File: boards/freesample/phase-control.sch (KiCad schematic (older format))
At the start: 45 parts, among them U16 HMC856, U17 NB6L295

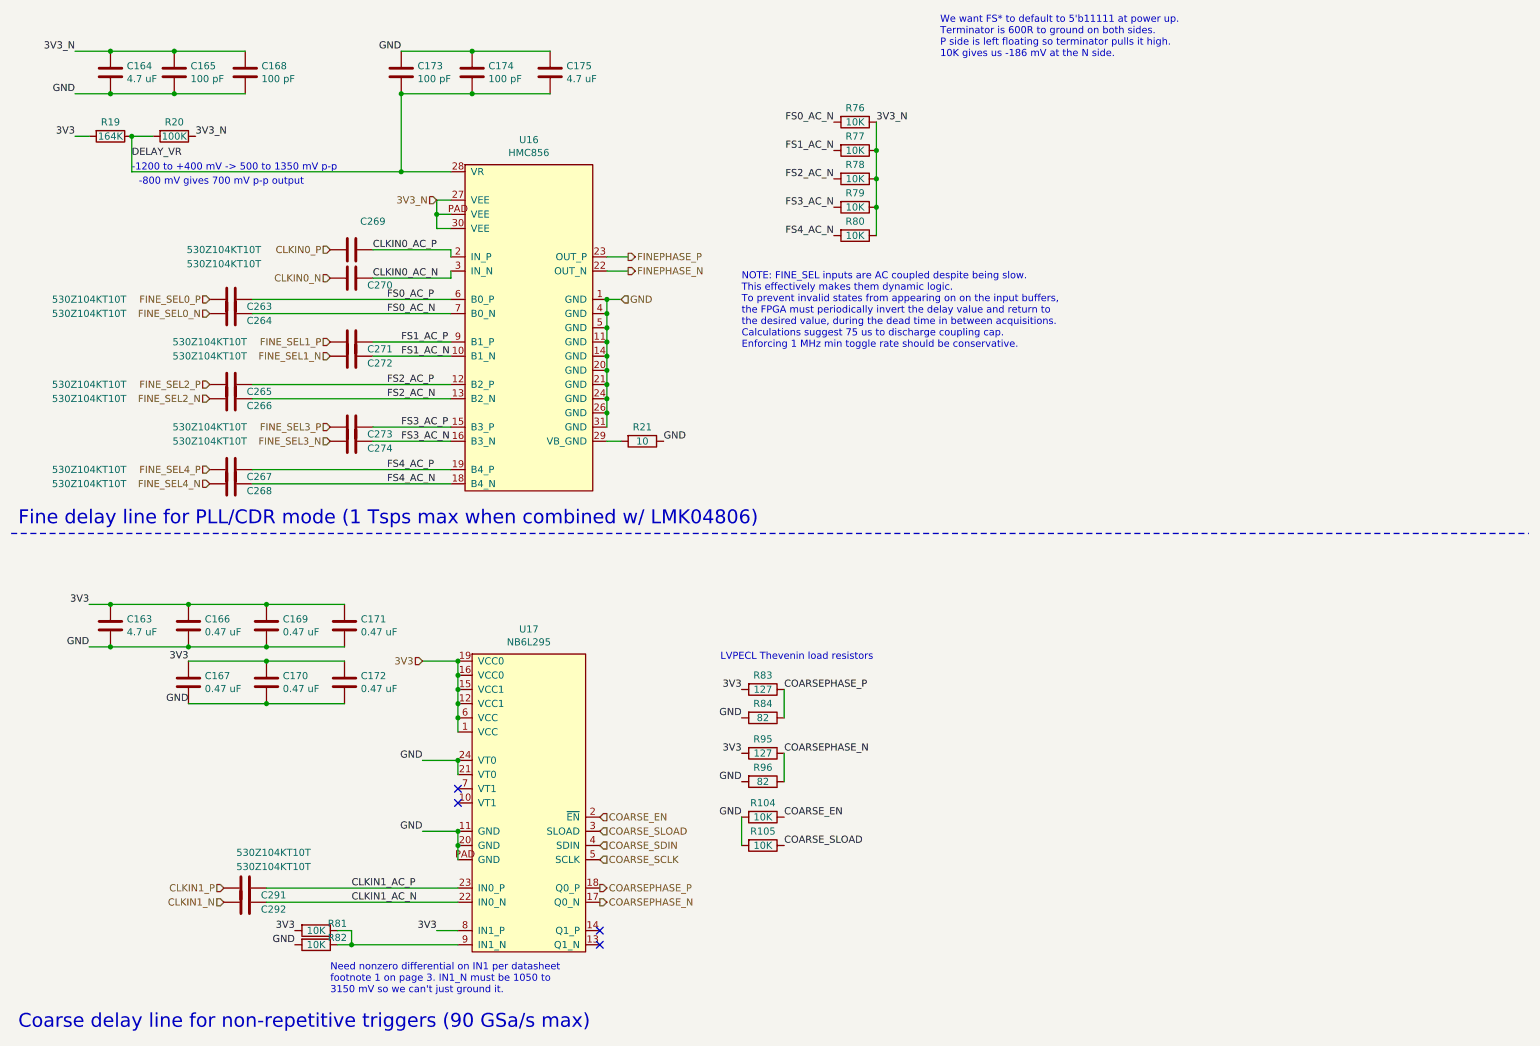
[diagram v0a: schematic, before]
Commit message: Added more test points. Started picking packages for passives. Continued schematic review.
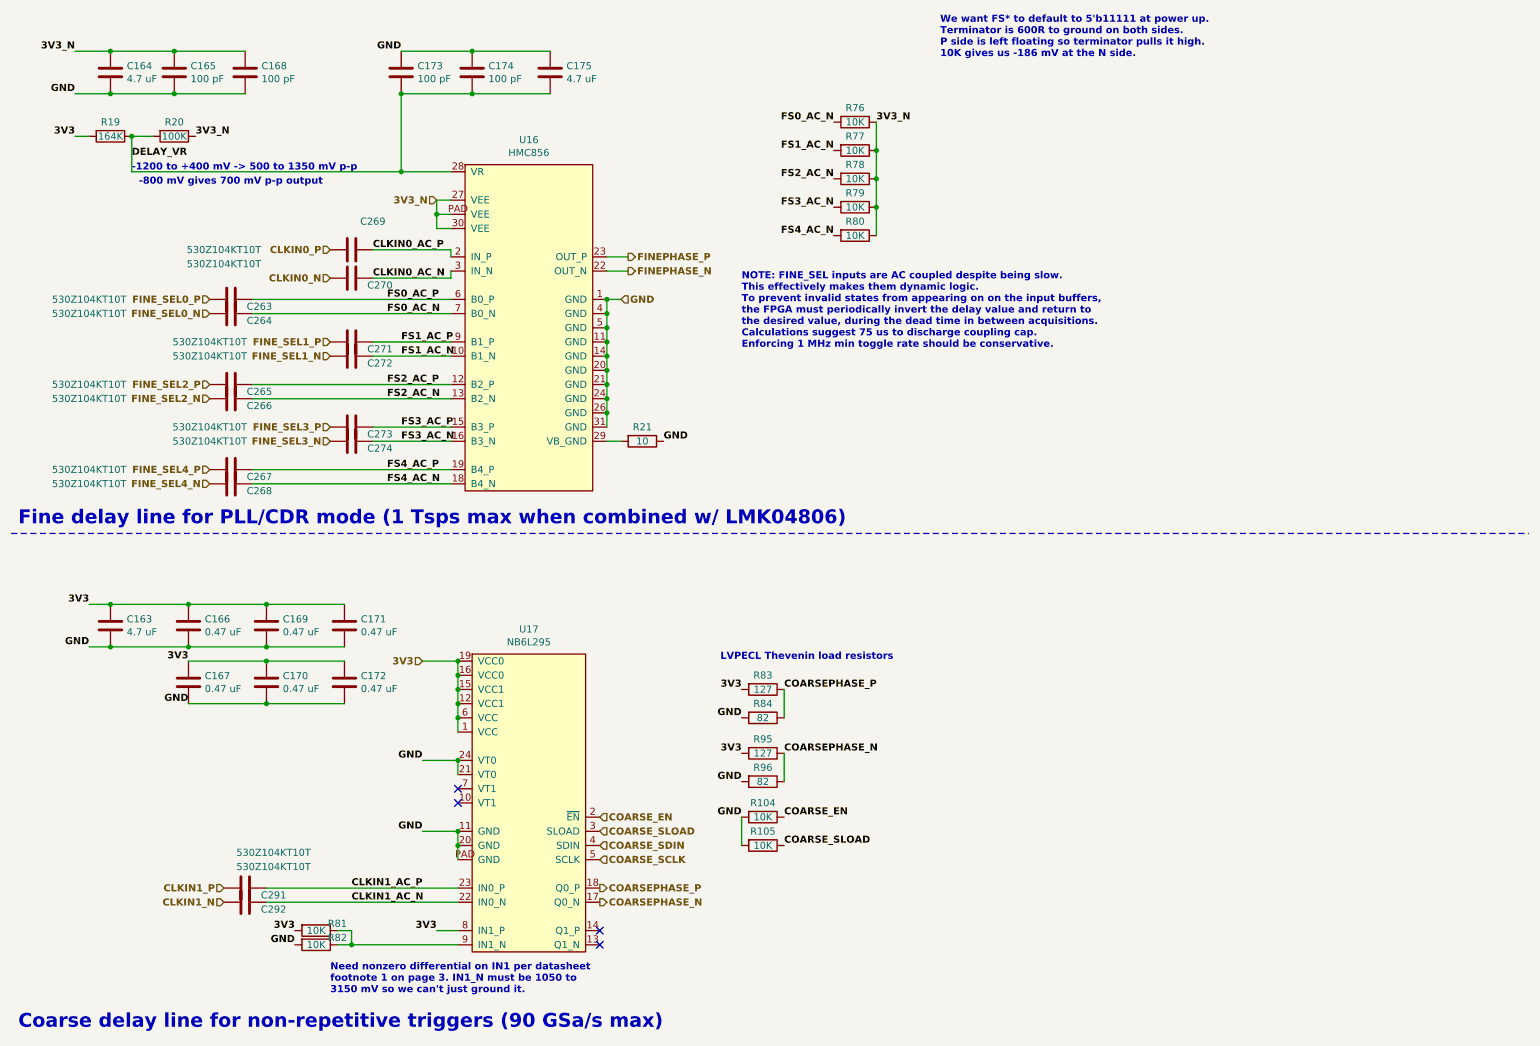
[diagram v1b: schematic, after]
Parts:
- C163, C164, C175: footprint (none) -> azonenberg_pcb:EIA_0603_CAP_NOSILK
- C165, C168, C173, C174, C263, C264, C265, C266, C267, C268, C269, C270, C271, C272, C273, C274, C291, C292: footprint (none) -> azonenberg_pcb:EIA_0201_CAP_NOSILK
- C166, C167, C169, C170, C171, C172: footprint (none) -> azonenberg_pcb:EIA_0402_CAP_NOSILK
- R104, R105, R76, R77, R78, R79, R80, R81, R82: footprint (none) -> azonenberg_pcb:EIA_0402_RES_NOSILK
- U16: footprint (none) -> azonenberg_pcb:QFN_32_0.5MM_5x5MM
- U17: footprint (none) -> azonenberg_pcb:QFN_24_0.5MM_4x4MM

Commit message: Continued assigning footprints
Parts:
- R19: value 164K -> 165K; footprint (none) -> azonenberg_pcb:EIA_0402_RES_NOSILK
- R20, R21, R83, R84, R95, R96: footprint (none) -> azonenberg_pcb:EIA_0402_RES_NOSILK
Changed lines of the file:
@@
 Sheet 12 12
 Title "FREESAMPLE Oscilloscope"
-Date "2019-03-15"
+Date "2019-03-16"
 Rev "0.1"
 Comp "Andrew D. Zonenberg / Antikernel Labs"
@@
 P 1200 1400
 F 0 "R19" V 1100 1400 50  0000 C CNN
-F 1 "164K" V 1200 1400 50  0000 C CNN
-F 2 "" V 1130 1400 50  0001 C CNN
+F 1 "165K" V 1200 1400 50  0000 C CNN
+F 2 "azonenberg_pcb:EIA_0402_RES_NOSILK" V 1130 1400 50  0001 C CNN
 F 3 "" H 1200 1400 50  0001 C CNN
 	1    1200 1400
@@
 F 0 "R20" V 1550 1400 50  0000 C CNN
 F 1 "100K" V 1650 1400 50  0000 C CNN
-F 2 "" V 1580 1400 50  0001 C CNN
+F 2 "azonenberg_pcb:EIA_0402_RES_NOSILK" V 1580 1400 50  0001 C CNN
 F 3 "" H 1650 1400 50  0001 C CNN
 	1    1650 1400
@@
 F 0 "R21" V 4850 3550 50  0000 C CNN
 F 1 "10" V 4950 3550 50  0000 C CNN
-F 2 "" V 4880 3550 50  0001 C CNN
+F 2 "azonenberg_pcb:EIA_0402_RES_NOSILK" V 4880 3550 50  0001 C CNN
 F 3 "" H 4950 3550 50  0001 C CNN
 	1    4950 3550
@@
 F 0 "R83" V 5700 5300 50  0000 C CNN
 F 1 "127" V 5800 5300 50  0000 C CNN
-F 2 "" V 5730 5300 50  0001 C CNN
+F 2 "azonenberg_pcb:EIA_0402_RES_NOSILK" V 5730 5300 50  0001 C CNN
 F 3 "" H 5800 5300 50  0001 C CNN
 	1    5800 5300
@@
 F 0 "R84" V 5700 5500 50  0000 C CNN
 F 1 "82" V 5800 5500 50  0000 C CNN
-F 2 "" V 5730 5500 50  0001 C CNN
+F 2 "azonenberg_pcb:EIA_0402_RES_NOSILK" V 5730 5500 50  0001 C CNN
 F 3 "" H 5800 5500 50  0001 C CNN
 	1    5800 5500
@@
 F 0 "R95" V 5700 5750 50  0000 C CNN
 F 1 "127" V 5800 5750 50  0000 C CNN
-F 2 "" V 5730 5750 50  0001 C CNN
+F 2 "azonenberg_pcb:EIA_0402_RES_NOSILK" V 5730 5750 50  0001 C CNN
 F 3 "" H 5800 5750 50  0001 C CNN
 	1    5800 5750
@@
 F 0 "R96" V 5700 5950 50  0000 C CNN
 F 1 "82" V 5800 5950 50  0000 C CNN
-F 2 "" V 5730 5950 50  0001 C CNN
+F 2 "azonenberg_pcb:EIA_0402_RES_NOSILK" V 5730 5950 50  0001 C CNN
 F 3 "" H 5800 5950 50  0001 C CNN
 	1    5800 5950

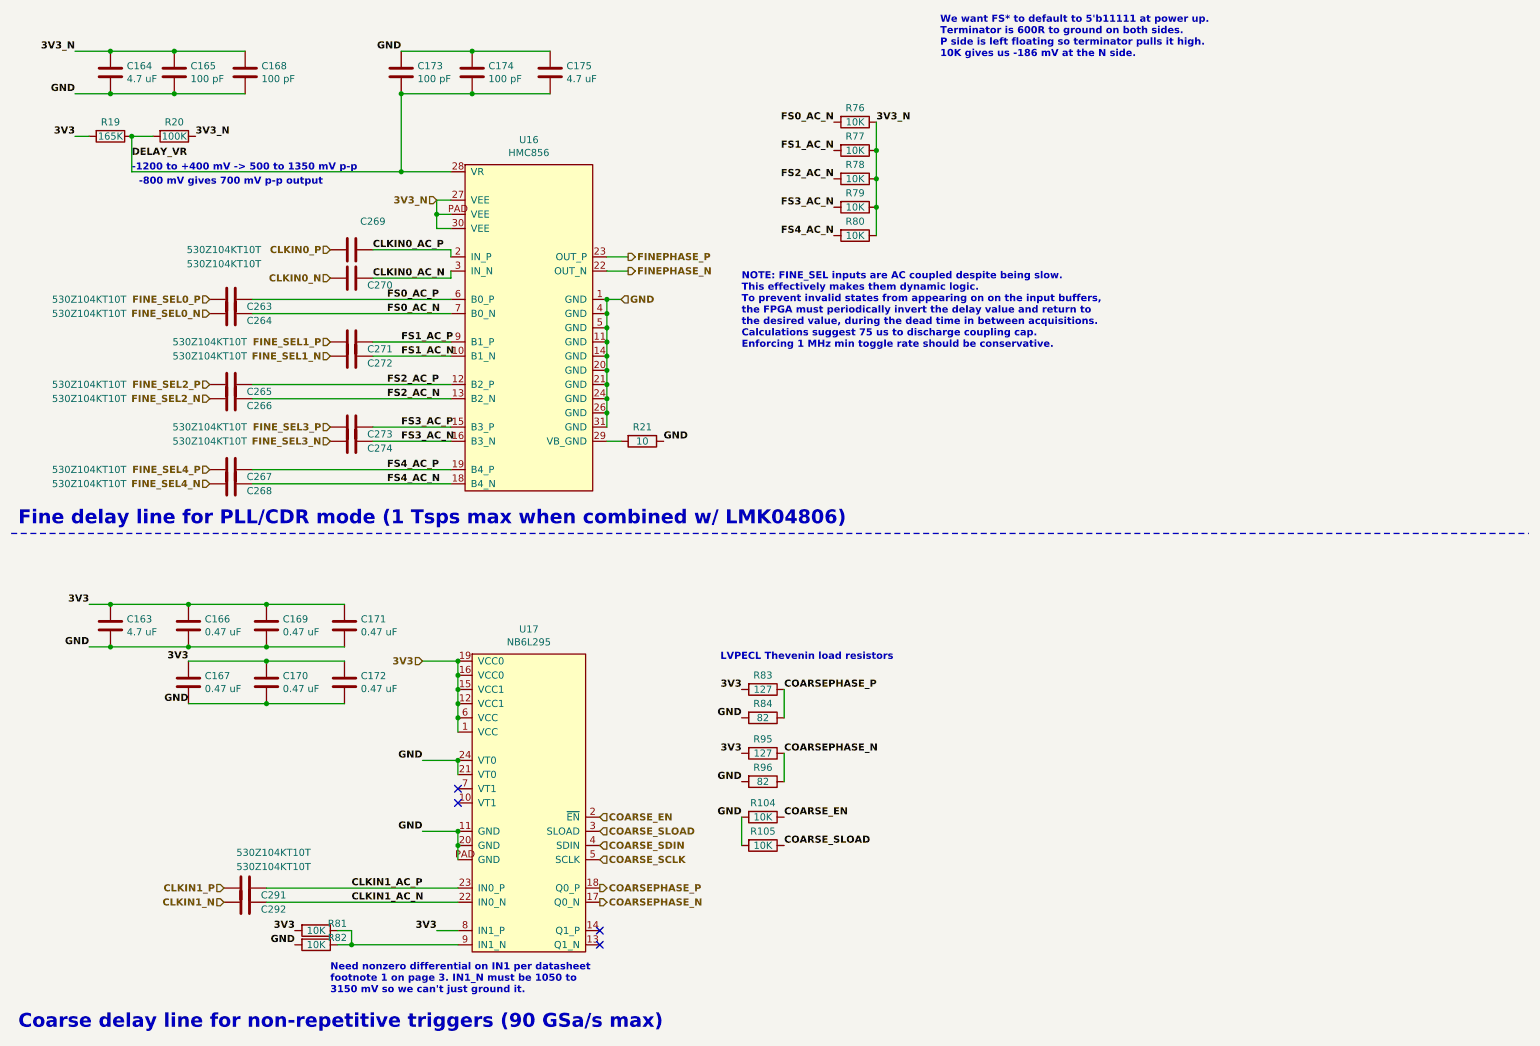
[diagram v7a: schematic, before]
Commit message: Initial layout of coarse delay line
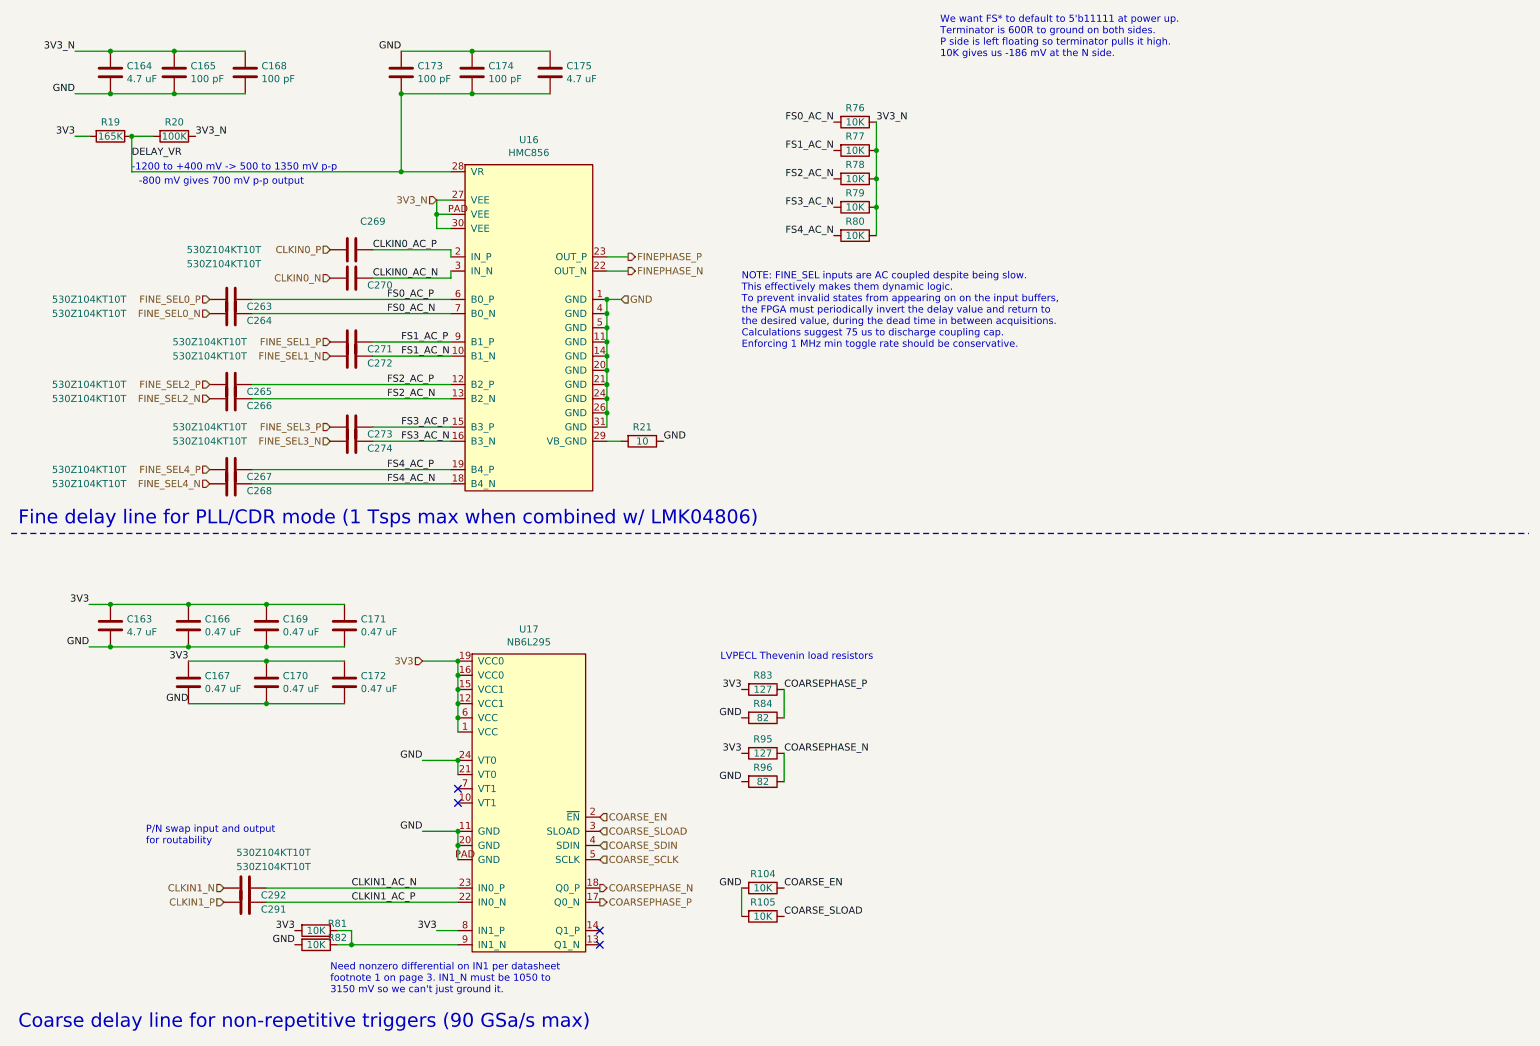
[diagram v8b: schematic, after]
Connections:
- net CLKIN1_AC_N: now also U17.23 (IN0_P); no longer U17.22 (IN0_N)
- net CLKIN1_AC_P: now also U17.22 (IN0_N); no longer U17.23 (IN0_P)
- net COARSEPHASE_N: now also U17.18 (Q0_P); no longer U17.17 (Q0_N)
- net COARSEPHASE_P: now also U17.17 (Q0_N); no longer U17.18 (Q0_P)
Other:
- note added: "P/N swap input and output\nfor routability"
- moved on the sheet: C291, C292, R104, R105
